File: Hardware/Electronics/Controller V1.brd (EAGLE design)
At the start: 91.4 x 91.7 mm, 18 parts, among them IC1 SN74AHCT125N, J1 POWER_JACK, J2 0039281023

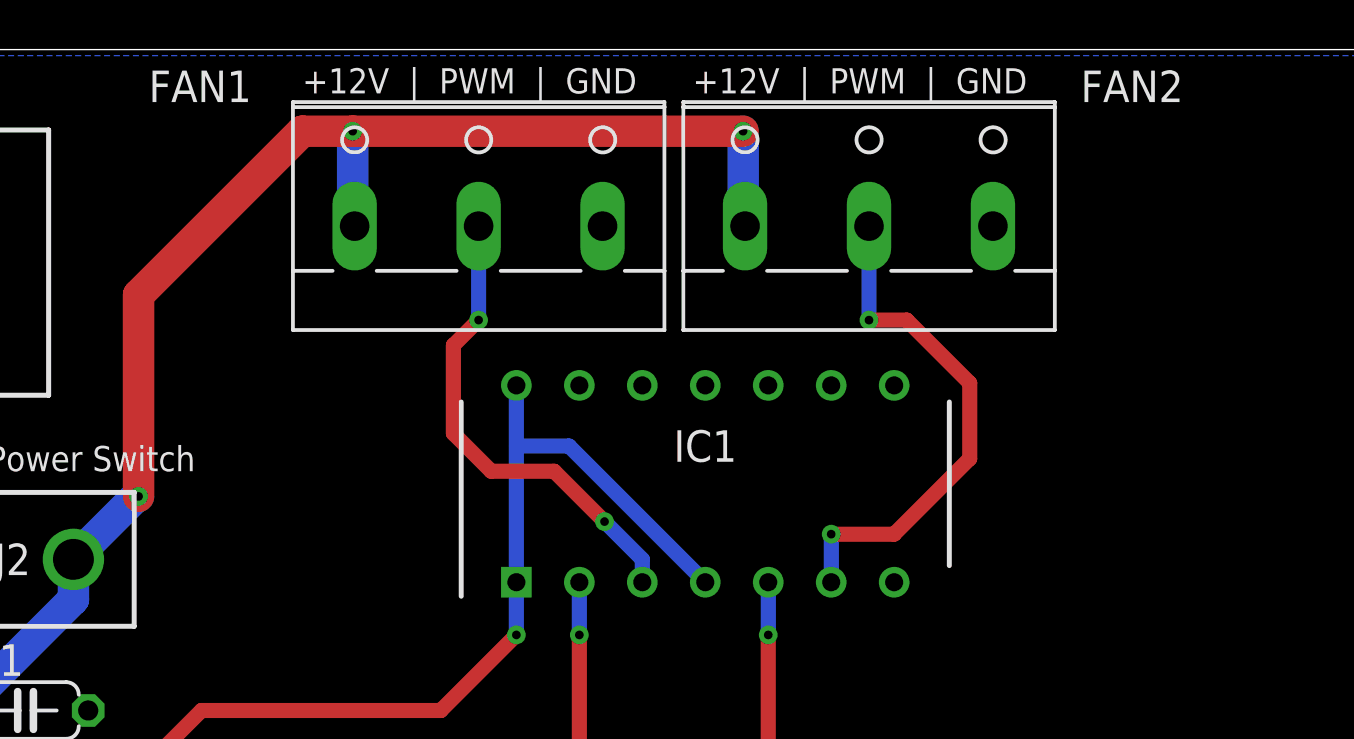
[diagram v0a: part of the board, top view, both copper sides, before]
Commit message: Changed screw terminals for actual 4 pin PWM fan headers
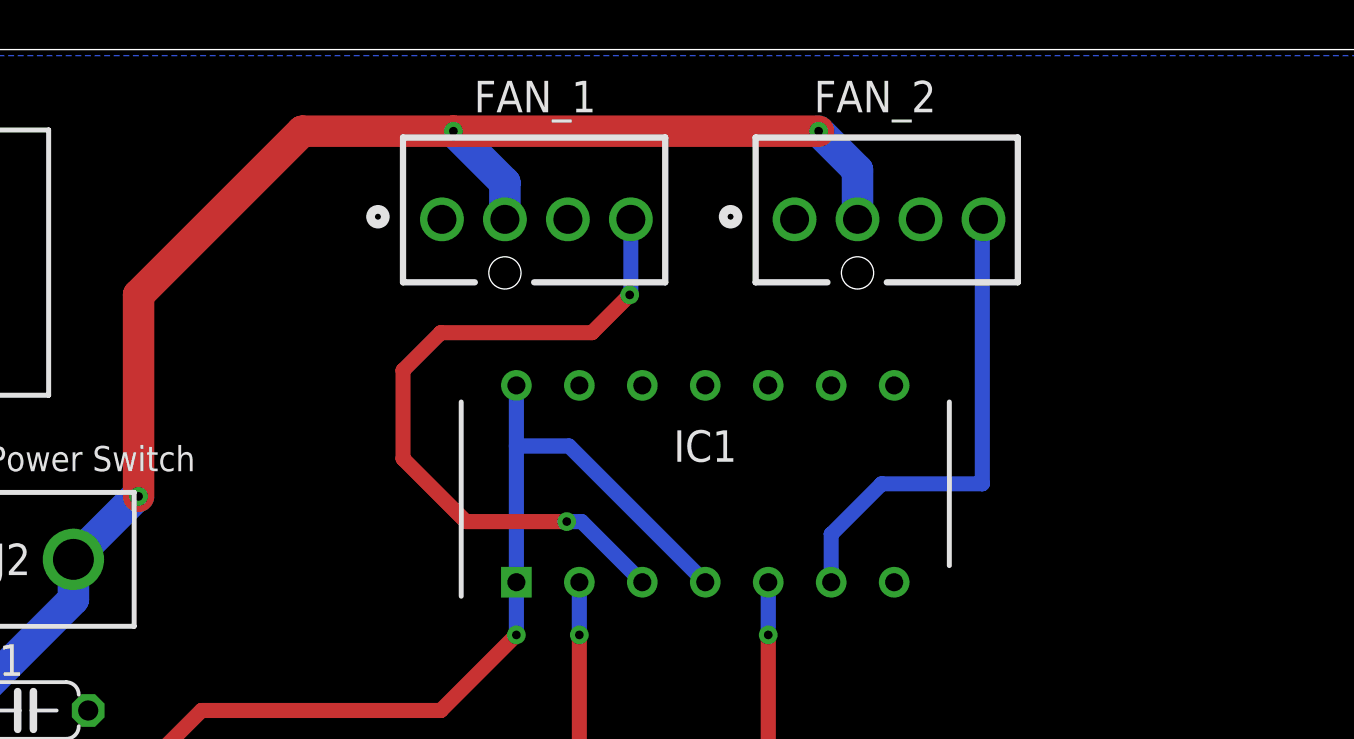
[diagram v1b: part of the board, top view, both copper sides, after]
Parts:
- removed FAN1, FAN2: (no value), con-wago-500:W237-103
- added FAN_1, FAN_2: 47053-1000, SamacSys_Parts:47053-1000
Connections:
- removed net FAN1_PWM_OUT: FAN1.2, IC1.3
- new net FAN!_PWM_OUT: FAN_1.4, IC1.3
- net +12V: now also FAN_1.2, FAN_2.2; no longer FAN1.1, FAN2.1
- net FAN2_PWM_OUT: now also FAN_2.4; no longer FAN2.2
- net GND: now also FAN_1.1, FAN_2.1; no longer FAN1.3, FAN2.3
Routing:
- net FAN!_PWM_OUT: track 0.00 -> 28.7 mm, vias 0 -> 2
- net FAN1_PWM_OUT: track 19.4 -> 0.00 mm, vias 2 -> 0
- net +12V: track 61.5 -> 65.2 mm
- net FAN2_PWM_OUT: track 21.0 -> 19.6 mm, vias 2 -> 0
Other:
- board text removed: "+12V | PWM | GND"
